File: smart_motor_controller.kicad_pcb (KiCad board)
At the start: 4 copper layers, 81 x 66 mm, 124 parts, among them J101 I2C_CONN, J102 SWD, J103 Input 12V, J104 Conn_02x07_Odd_Even, J301 M0_CONN, J302 M0_CONN, J303 M0_CONN, J304 M0_CONN, J401 Encoder Connector 0, J402 Encoder Connector 1, J403 Encoder Connector 2, J404 Encoder Connector 3, J405 External encoders power, J501 USB_C_Receptacle_USB2.0_16P, SW101 SW_NRST, SW102 SW_NRST, U101 STM32F405VGTx, U201 TPS54331DDAR, U301 DRV8873S, U302 DRV8873S, U303 DRV8873S, U304 DRV8873S, U501 USBLC6-2SC6, U601 BMI088, U602 TMP102xxDRL

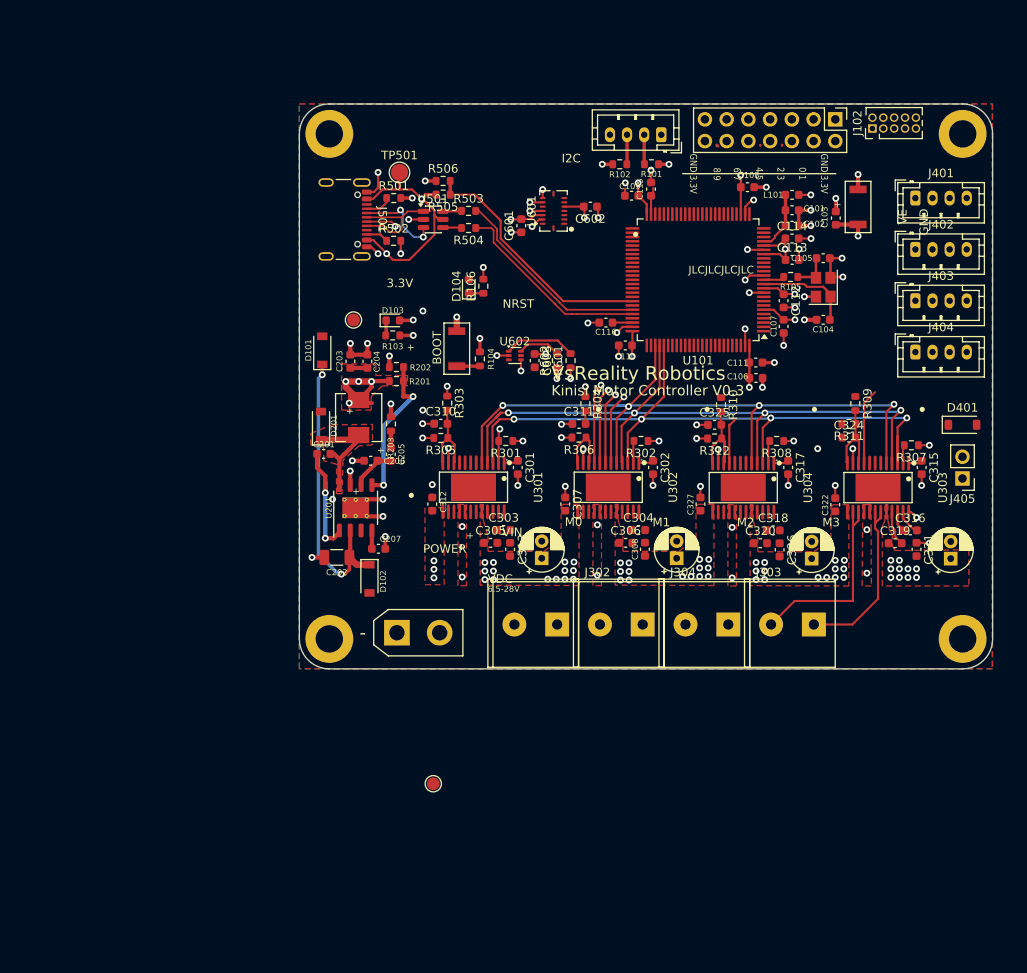
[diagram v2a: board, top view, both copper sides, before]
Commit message: Implement structure for code changes tracking
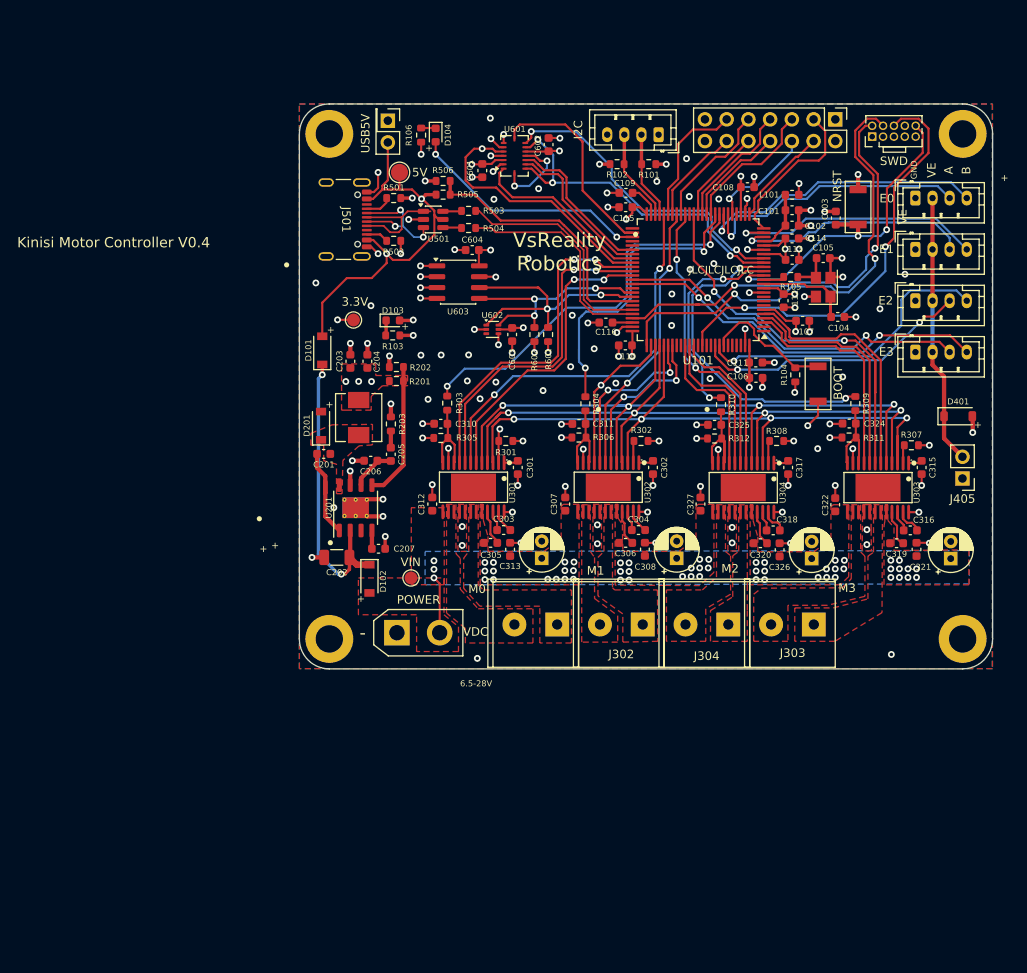
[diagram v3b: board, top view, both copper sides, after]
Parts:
- added C604: 100nf, Capacitor_SMD:C_0603_1608Metric, F.Cu at (143.2, 72.6)
- added U603: FM24C64B, Package_SO:SOIC-8_3.9x4.9mm_P1.27mm, F.Cu at (141.6, 76.3)
- added USB5V: USB_5V, Connector_PinHeader_2.54mm:PinHeader_2x01_P2.54mm_Vertical, F.Cu at (133.3, 57.5)
- moved SW102 42.4 mm to (183.6, 88.2), turned to -90 degrees
- moved R104 36.9 mm to (181.0, 87.2), turned to 90 degrees
- moved TP101 24.2 mm to (136.1, 110.9)
- moved R106 19.1 mm to (137.2, 59.1), turned to -90 degrees
- moved D104 18.1 mm to (138.9, 59.1), turned to -90 degrees
- moved C602 8.74 mm to (152.1, 60.2), turned to -90 degrees
- moved C601 7.89 mm to (144.4, 63.3)
- moved U601 7.89 mm to (148.1, 61.6)
- moved U602 4.03 mm to (145.6, 81.8)
- moved C603 4.03 mm to (147.9, 82.5)
- moved R601 4.03 mm to (152.1, 82.5)
- moved R602 4.03 mm to (150.5, 82.5)
- moved C115 2.97 mm to (161.2, 65.9), turned to 180 degrees
- moved C107 2.32 mm to (181.8, 80.8), turned to 0 degrees
- moved C104 1.73 mm to (185.9, 80.4), turned to 0 degrees
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- renumbered TP501 to 5V, J401 to E0, J402 to E1, J403 to E2, J404 to E3, J102 to SWD
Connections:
- J101 pad 2: I2C2_SCL -> I2C_E_SCL
- J101 pad 3: I2C2_SDA -> I2C_E_SDA
- J104 pad 10: GPIO1 -> GPIO3
- J104 pad 11: I2C1_SDA -> GPIO0
- J104 pad 12: I2C1_SCL -> GPIO1
- J104 pad 3: CAN2_TX -> USART_E_TX
- J104 pad 4: CAN2_RX -> USART_E_RX
- J104 pad 5: USART3_TX -> GPIO6
- J104 pad 6: USART3_RX -> GPIO7
- J104 pad 7: GPIO2 -> GPIO4
- J104 pad 8: GPIO3 -> GPIO5
- J104 pad 9: GPIO0 -> GPIO2
- R101 pad 2: I2C2_SCL -> I2C_E_SCL
- R102 pad 2: I2C2_SDA -> I2C_E_SDA
- U101 pad 15: unconnected-(U101-PC0-Pad15) -> M2_IPROPI
- U101 pad 16: unconnected-(U101-PC1-Pad16) -> M3_IPROPI
- U101 pad 25: LED -> USART_E_TX
- U101 pad 26: unconnected-(U101-PA3-Pad26) -> USART_E_RX
- U101 pad 3: unconnected-(U101-PE4-Pad3) -> M3_DISABLE
- U101 pad 30: unconnected-(U101-PA5-Pad30) -> GPIO7
- U101 pad 33: unconnected-(U101-PC4-Pad33) -> M0_IPROPI
- U101 pad 34: unconnected-(U101-PC5-Pad34) -> M1_IPROPI
- U101 pad 35: unconnected-(U101-PB0-Pad35) -> GPIO6
- U101 pad 36: unconnected-(U101-PB1-Pad36) -> GPIO5
- U101 pad 37: unconnected-(U101-PB2-Pad37) -> GPIO4
- U101 pad 38: unconnected-(U101-PE7-Pad38) -> GPIO3
- U101 pad 39: M0_EN -> M3_EN
- U101 pad 4: unconnected-(U101-PE5-Pad4) -> M3_PH
- U101 pad 41: M1_EN -> M2_EN
- U101 pad 42: unconnected-(U101-PE11-Pad42) -> GPIO2
- U101 pad 43: M2_EN -> M1_EN
- U101 pad 44: unconnected-(U101-PE13-Pad44) -> GPIO1
- U101 pad 45: unconnected-(U101-PE14-Pad45) -> GPIO0
- U101 pad 46: M3_EN -> M0_EN
- U101 pad 47: IMU_SCK -> I2C_E_SCL
- U101 pad 48: unconnected-(U101-PB11-Pad48) -> I2C_E_SDA
- U101 pad 5: unconnected-(U101-PE6-Pad5) -> M3_nSCS
- U101 pad 52: unconnected-(U101-PB13-Pad52) -> IMU_SCK
- U101 pad 53: unconnected-(U101-PB14-Pad53) -> LED
- U101 pad 56: unconnected-(U101-PD9-Pad56) -> IMU_INT_GYRO
- U101 pad 57: unconnected-(U101-PD10-Pad57) -> IMU_CSB1_ACCEL
- U101 pad 58: unconnected-(U101-PD11-Pad58) -> IMU_INT_ACCEL
- U101 pad 59: unconnected-(U101-PD12-Pad59) -> IMU_CSB1_GYRO
- U101 pad 60: unconnected-(U101-PD13-Pad60) -> M0_DISABLE
- U101 pad 61: unconnected-(U101-PD14-Pad61) -> M0_PH
- U101 pad 62: unconnected-(U101-PD15-Pad62) -> M0_nSCS
- U101 pad 77: unconnected-(U101-PA15-Pad77) -> M1_DISABLE
- U101 pad 81: unconnected-(U101-PD0-Pad81) -> M1_PH
- U101 pad 82: unconnected-(U101-PD1-Pad82) -> M1_nSCS
- U101 pad 85: unconnected-(U101-PD4-Pad85) -> M2_DISABLE
- U101 pad 86: unconnected-(U101-PD5-Pad86) -> M2_PH
- U101 pad 87: unconnected-(U101-PD6-Pad87) -> M2_nSCS
- U601 pad 1: IMU_INT2_ACCEL -> IMU_INT_ACCEL
- U601 pad 12: IMU_INT3_GYRO -> Net-(U601-INT1)
- U601 pad 13: IMU_INT4_GYRO -> IMU_INT_GYRO
- U601 pad 16: IMU_INT1_ACCEL -> Net-(U601-INT1)
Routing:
- net SWCLK: track 0.00 -> 54.7 mm, vias 0 -> 2
- net SWO: track 0.00 -> 50.3 mm, vias 0 -> 2
- net SWDIO: track 0.00 -> 49.9 mm, vias 0 -> 2
- net M3_EN: track 0.00 -> 48.0 mm, vias 0 -> 2
- net M0_EN: track 0.00 -> 46.3 mm, vias 0 -> 2
- net M0_IPROPI: track 1.15 -> 45.8 mm, vias 1 -> 2
- net ENCODER_3_B: track 0.00 -> 44.1 mm, vias 0 -> 2
- net ENCODER_3_A: track 0.00 -> 41.9 mm, vias 0 -> 2
- net IMU_MISO: track 0.00 -> 41.2 mm, vias 0 -> 3
- net M0_DISABLE: track 0.00 -> 40.5 mm, vias 0 -> 2
- net M3_IPROPI: track 0.00 -> 39.1 mm, vias 0 -> 2
- net M0_PH: track 0.00 -> 38.9 mm, vias 0 -> 2
- net IMU_SDI: track 0.00 -> 36.7 mm, vias 0 -> 2
- net ENCODER_2_B: track 0.00 -> 35.9 mm, vias 0 -> 1
- net M1_IPROPI: track 1.17 -> 36.7 mm, vias 1 -> 2
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- added copper zone on F.Cu, net Net-(J301-Pin_1)
- added copper zone on F.Cu, net Net-(J301-Pin_2)
- added copper zone on F.Cu, net Net-(J302-Pin_1)
- added copper zone on F.Cu, net Net-(J302-Pin_2)
- added copper zone on F.Cu, net Net-(J303-Pin_1)
- added copper zone on F.Cu, net Net-(J303-Pin_2)
- added copper zone on F.Cu, net Net-(J304-Pin_1)
- added copper zone on F.Cu, net Net-(J304-Pin_2)
- added copper zone on B.Cu, net VMOTORS
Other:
- board text added: "A"
- board text added: "B"
- board text added: "Kinisi Motor Controller V0.4"
- board text removed: "0 1"
- board text removed: "1 0"
- board text removed: "2 3"
- board text removed: "3 2"
- board text removed: "3.3V GND"
- board text removed: "4 5"
- board text removed: "5 4"
- board text removed: "6 7"
- board text removed: "7 6"
- board text removed: "8 9"
- board text removed: "9 8"
- board text removed: "GND 3.3V"
- board text removed: "Kinisi Motor Controller V0.3"
